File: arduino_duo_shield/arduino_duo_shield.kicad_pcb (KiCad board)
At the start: 2 copper layers, 101.6 x 53.3 mm, 13 parts, among them P1 Digital, P10 CONN_01X01, P11 CONN_01X01, P12 CONN_01X01, P13 CONN_01X01, P2 Power, P3 Analog, P4 Analog, P5 PWM, P6 PWM, P7 Communication, P8 CONN_01X01, P9 CONN_01X01

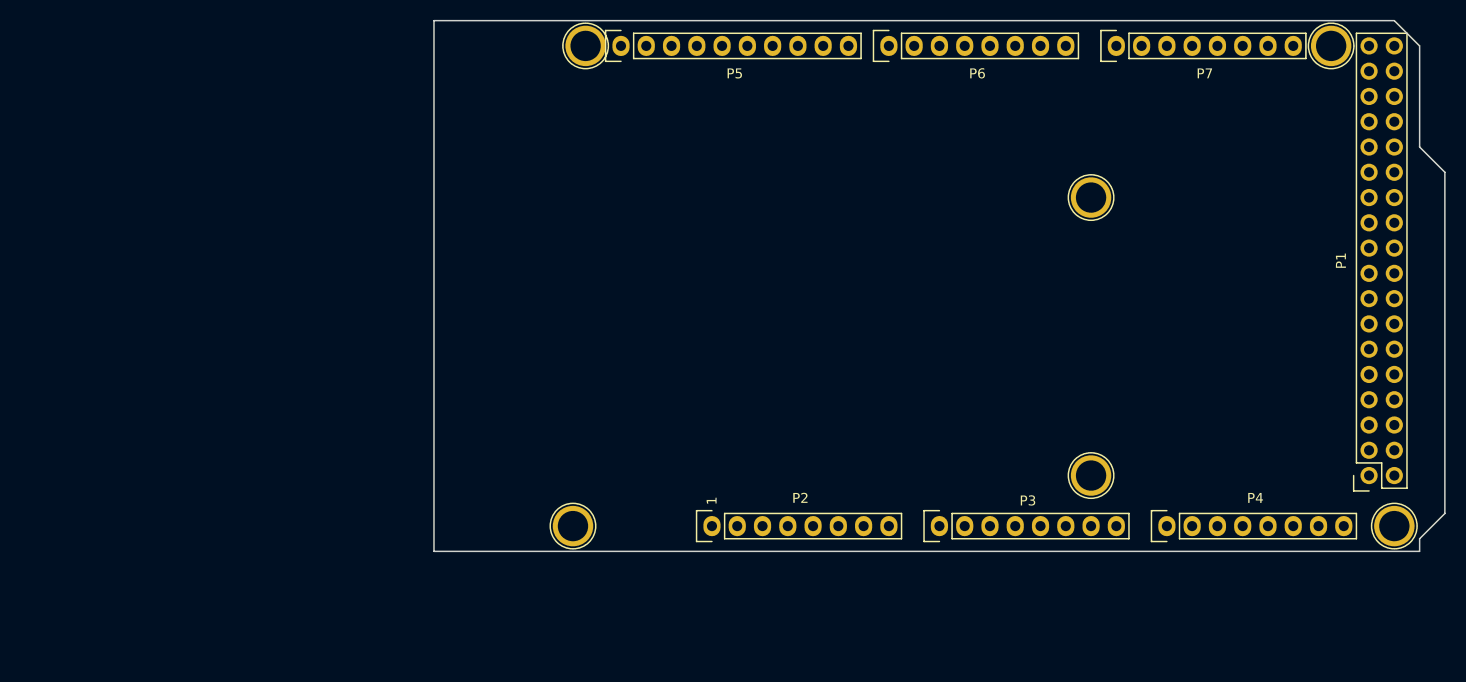
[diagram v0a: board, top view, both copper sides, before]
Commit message: Add labels and footprints
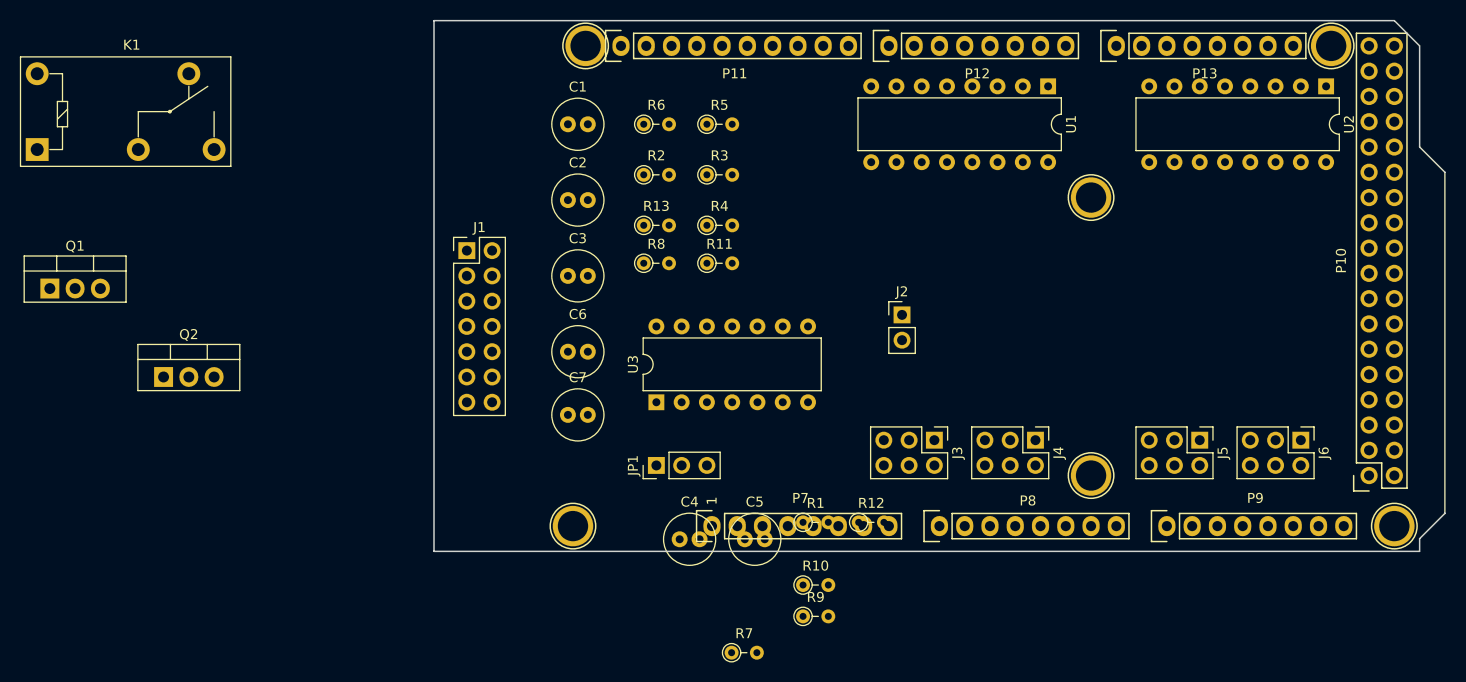
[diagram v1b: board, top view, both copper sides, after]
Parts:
- added C1: 100nF, Capacitor_THT:C_Radial_D5.0mm_H11.0mm_P2.00mm, F.Cu at (116.8, 78.7)
- added C2: 100nF, Capacitor_THT:C_Radial_D5.0mm_H11.0mm_P2.00mm, F.Cu at (116.8, 86.4)
- added C3: 100nF, Capacitor_THT:C_Radial_D5.0mm_H11.0mm_P2.00mm, F.Cu at (116.8, 94.0)
- added C4: 100nF, Capacitor_THT:C_Radial_D5.0mm_H11.0mm_P2.00mm, F.Cu at (128.1, 120.5)
- added C5: 100nF, Capacitor_THT:C_Radial_D5.0mm_H11.0mm_P2.00mm, F.Cu at (134.6, 120.5)
- added C6: 100nF, Capacitor_THT:C_Radial_D5.0mm_H11.0mm_P2.00mm, F.Cu at (116.8, 101.6)
- added C7: 100pF, Capacitor_THT:C_Radial_D5.0mm_H11.0mm_P2.00mm, F.Cu at (116.8, 108.0)
- added J1: Conn_02x07_Counter_Clockwise, Connector_PinHeader_2.54mm:PinHeader_2x07_P2.54mm_Vertical, F.Cu at (106.7, 91.4)
- added J2: Conn_01x02_Male, Connector_PinHeader_2.54mm:PinHeader_1x02_P2.54mm_Vertical, F.Cu at (150.4, 97.9)
- added J3: Conn_02x03_Counter_Clockwise, Connector_PinHeader_2.54mm:PinHeader_2x03_P2.54mm_Vertical, F.Cu at (153.7, 110.5)
- added J4: Conn_02x03_Counter_Clockwise, Connector_PinHeader_2.54mm:PinHeader_2x03_P2.54mm_Vertical, F.Cu at (163.8, 110.5)
- added J5: Conn_02x03_Counter_Clockwise, Connector_PinHeader_2.54mm:PinHeader_2x03_P2.54mm_Vertical, F.Cu at (180.3, 110.5)
- added J6: Conn_02x03_Counter_Clockwise, Connector_PinHeader_2.54mm:PinHeader_2x03_P2.54mm_Vertical, F.Cu at (190.5, 110.5)
- added JP1: Jumper_3_Bridged12, Connector_PinHeader_2.54mm:PinHeader_1x03_P2.54mm_Vertical, F.Cu at (125.7, 113.0)
- added K1: G5Q-1, Relay_THT:Relay_SPDT_Omron-G5Q-1, F.Cu at (63.5, 81.3)
- added Q1: IRFZ44N, Package_TO_SOT_THT:TO-220-3_Vertical, F.Cu at (64.8, 95.2)
- added Q2: IRFZ44N, Package_TO_SOT_THT:TO-220-3_Vertical, F.Cu at (76.2, 104.1)
- added R1: 10K, Resistor_THT:R_Axial_DIN0204_L3.6mm_D1.6mm_P2.54mm_Vertical, F.Cu at (140.5, 118.8)
- added R10: 10K, Resistor_THT:R_Axial_DIN0204_L3.6mm_D1.6mm_P2.54mm_Vertical, F.Cu at (140.5, 125.0)
- added R11: 10K, Resistor_THT:R_Axial_DIN0204_L3.6mm_D1.6mm_P2.54mm_Vertical, F.Cu at (130.8, 92.7)
- added R12: 10K, Resistor_THT:R_Axial_DIN0204_L3.6mm_D1.6mm_P2.54mm_Vertical, F.Cu at (146.1, 118.8)
- added R13: 10K, Resistor_THT:R_Axial_DIN0204_L3.6mm_D1.6mm_P2.54mm_Vertical, F.Cu at (124.5, 88.9)
- added R2: 10K, Resistor_THT:R_Axial_DIN0204_L3.6mm_D1.6mm_P2.54mm_Vertical, F.Cu at (124.5, 83.8)
- added R3: 10K, Resistor_THT:R_Axial_DIN0204_L3.6mm_D1.6mm_P2.54mm_Vertical, F.Cu at (130.8, 83.8)
- added R4: 10K, Resistor_THT:R_Axial_DIN0204_L3.6mm_D1.6mm_P2.54mm_Vertical, F.Cu at (130.8, 88.9)
- added R5: 10K, Resistor_THT:R_Axial_DIN0204_L3.6mm_D1.6mm_P2.54mm_Vertical, F.Cu at (130.8, 78.7)
- added R6: 10K, Resistor_THT:R_Axial_DIN0204_L3.6mm_D1.6mm_P2.54mm_Vertical, F.Cu at (124.5, 78.7)
- added R7: 10K, Resistor_THT:R_Axial_DIN0204_L3.6mm_D1.6mm_P2.54mm_Vertical, F.Cu at (133.3, 131.8)
- added R8: 10K, Resistor_THT:R_Axial_DIN0204_L3.6mm_D1.6mm_P2.54mm_Vertical, F.Cu at (124.5, 92.7)
- added R9: 10K, Resistor_THT:R_Axial_DIN0204_L3.6mm_D1.6mm_P2.54mm_Vertical, F.Cu at (140.5, 128.2)
- added U1: 4504, Package_DIP:DIP-16_W7.62mm, F.Cu at (165.1, 74.9)
- added U2: 4504, Package_DIP:DIP-16_W7.62mm, F.Cu at (193.0, 74.9)
- added U3: 74HC14, Package_DIP:DIP-14_W7.62mm, F.Cu at (125.7, 106.7)
- renumbered P8 to P1, P1 to P10, P5 to P11, P6 to P12, P7 to P13, P9 to P2, P10 to P3, P11 to P4, P12 to P5, P13 to P6, P2 to P7, P3 to P8, P4 to P9
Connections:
- P10 pad 23: /32 -> m4dir
- P10 pad 24: /33 -> m4enab
- P10 pad 26: /31 -> m4step
- P10 pad 27: /28 -> m3enab
- P10 pad 32: /25 -> m2enab
- P10 pad 33: /22 -> m1enab
- P11 pad 6: /12(**) -> spenab
- P11 pad 7: /11(**) -> sppwm
- P12 pad 1: /7(**) -> m3dir
- P12 pad 2: /6(**) -> m2dir
- P12 pad 3: /5(**) -> m1dir
- P12 pad 4: /4(**) -> m3step
- P12 pad 5: /3(**) -> m2step
- P12 pad 6: /2(**) -> m1step
- P13 pad 1: /14(Tx3) -> Xmn
- P13 pad 2: /15(Rx3) -> Xmx
- P13 pad 3: /16(Tx2) -> Ymn
- P13 pad 4: /17(Rx2) -> Ymx
- P13 pad 5: /18(Tx1) -> Zmn
- P13 pad 6: /19(Rx1) -> Zmx
- P8 pad 8: /A7 -> Probe
